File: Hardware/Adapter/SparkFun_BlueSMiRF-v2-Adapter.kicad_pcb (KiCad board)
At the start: 2 copper layers, 22.2 x 15.2 mm, 9 parts, among them J1 JST_Locking_6, J2 Conn_01x06, J3 Conn_01x06

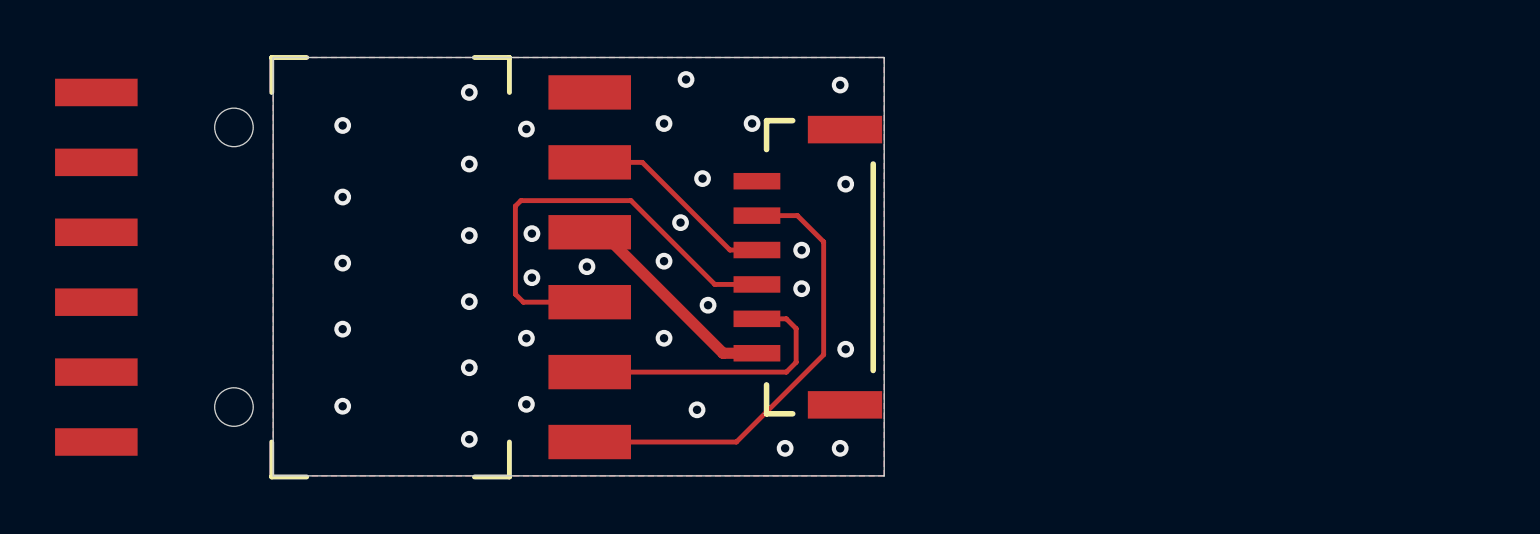
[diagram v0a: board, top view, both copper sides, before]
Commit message: Make backwards compatible
Earlier boards had RX and TX lines swapped
- Adds switches on RX/TX lines
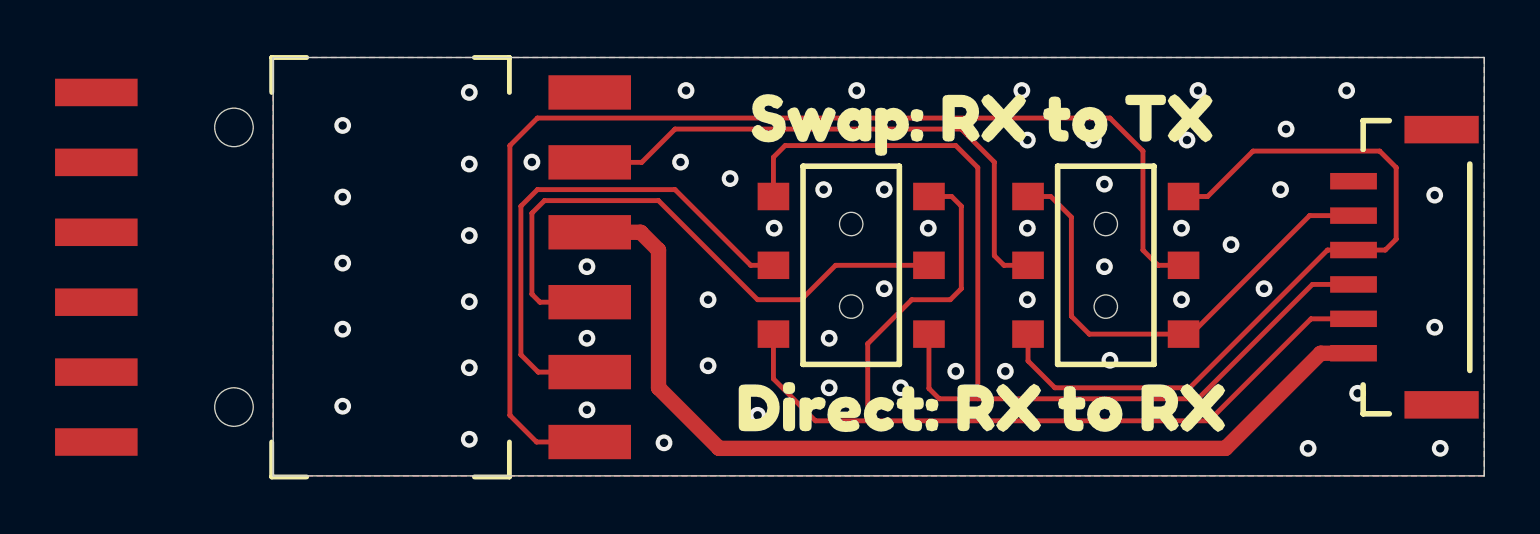
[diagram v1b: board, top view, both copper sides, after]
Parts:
- added SW1: DPDT_Slide_SMD_7.2x3.5mm, SparkFun-Switch:Slide_DPDT_SMD_7.2x3.5mm, F.Cu at (127.6, 83.2)
- added SW2: DPDT_Slide_SMD_7.2x3.5mm, SparkFun-Switch:Slide_DPDT_SMD_7.2x3.5mm, F.Cu at (136.8, 83.2)
- added kibuzzard-688F940F: G***, kibuzzard-688F940F, B.Cu at (146.9, 77.0)
- added kibuzzard-688F9569: G***, kibuzzard-688F9569, B.Cu at (146.5, 79.5)
- added kibuzzard-688F9588: G***, kibuzzard-688F9588, B.Cu at (146.6, 87.0)
- added kibuzzard-688F95BB: G***, kibuzzard-688F95BB, B.Cu at (146.6, 84.7)
- added kibuzzard-688F95E9: G***, kibuzzard-688F95E9, B.Cu at (146.5, 82.2)
- added kibuzzard-688F95F7: G***, kibuzzard-688F95F7, B.Cu at (146.9, 89.4)
- added kibuzzard-688F9C93: G***, kibuzzard-688F9C93, F.Cu at (132.3, 88.3)
- added kibuzzard-688F9D85: G***, kibuzzard-688F9D85, F.Cu at (132.3, 78.0)
- moved J1 21.7 mm to (147.6, 83.2)
- moved kibuzzard-6880B6C0 0.05 mm to (110.2, 82.1)
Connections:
- J1 pad 2: RXI -> RX
- J1 pad 3: TXO -> TX
- J1 pad 4: ~{CTS} -> CTS
- J1 pad 5: ~{RTS} -> RTS
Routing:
- net TX: track 0.00 -> 37.0 mm
- net RX: track 0.00 -> 36.2 mm
- net CTS: track 0.00 -> 28.2 mm
- net VCC: track 7.90 -> 35.4 mm
- net ~{RTS}: track 16.7 -> 42.3 mm
- net RTS: track 0.00 -> 17.8 mm
- net ~{CTS}: track 7.39 -> 20.5 mm
- net RXI: track 10.4 -> 18.7 mm
- net TXO: track 16.1 -> 21.8 mm
- net GND: vias 33 -> 55
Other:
- board size 22.2 x 15.2 mm -> 44 x 15.2 mm
